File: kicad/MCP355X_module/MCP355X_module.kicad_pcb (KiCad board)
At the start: 2 copper layers, 20.8 x 20.8 mm, 21 parts, among them J1 PINS_1X8, J2 PINS_1X8, U1 MCP355X-E_SN

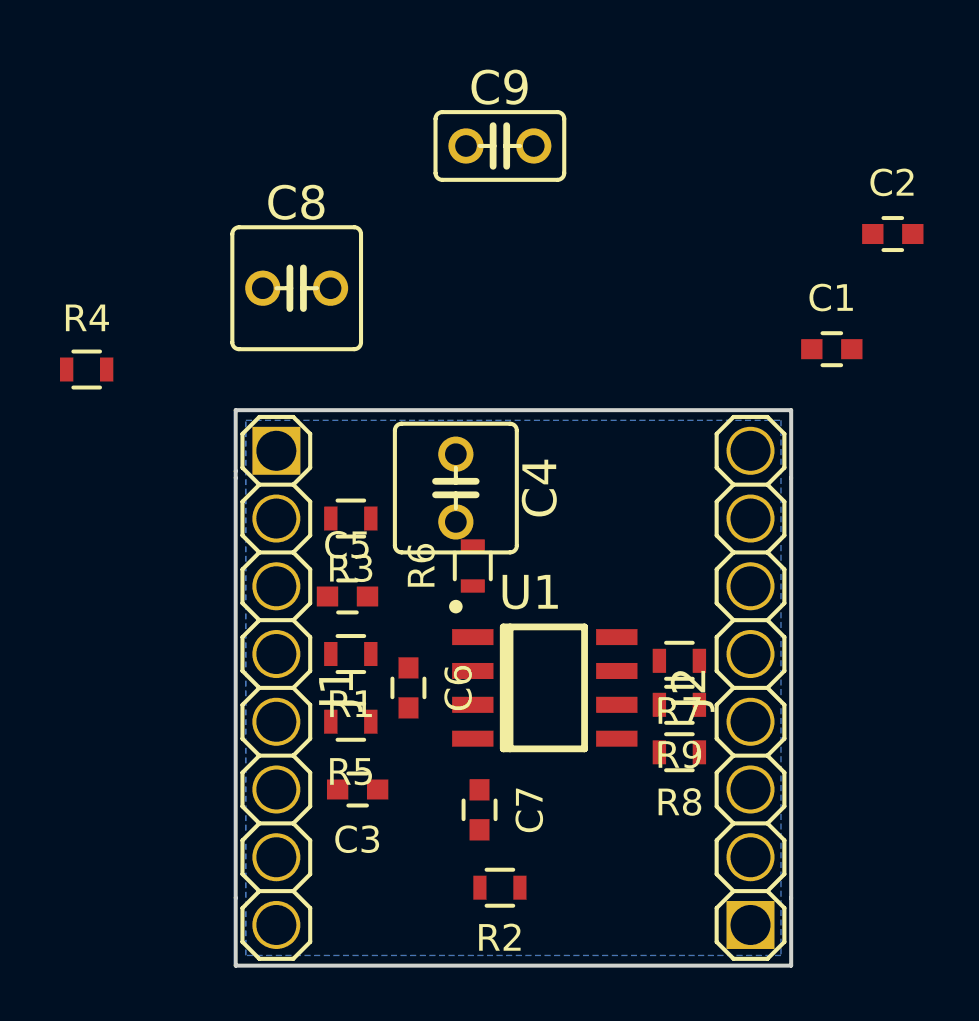
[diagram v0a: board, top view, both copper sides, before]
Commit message: * finished routing MCP355X PCB
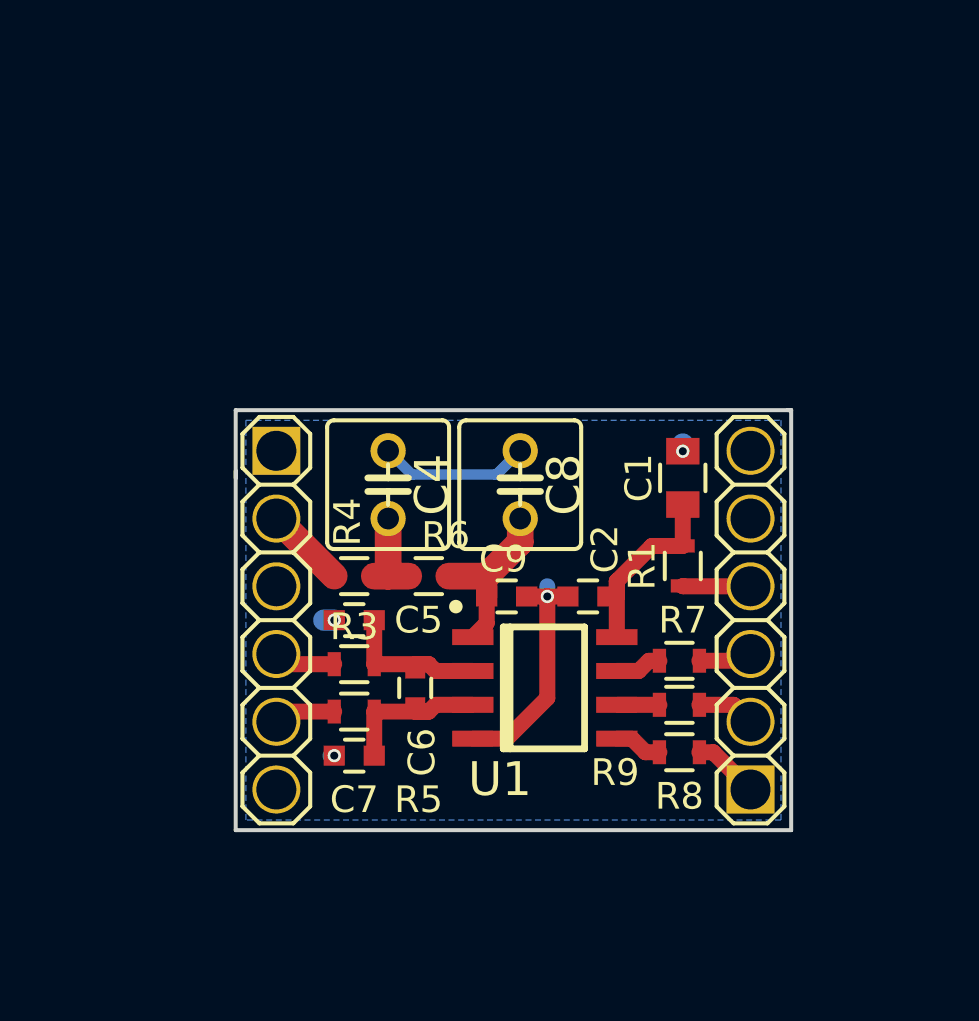
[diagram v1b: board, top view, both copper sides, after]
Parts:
- removed C3: C, Capacitors_SMD:C_0603
- removed R2: R, Resistors_SMD:R_0603
- C1: value C -> 1u; footprint Capacitors_SMD:C_0603 -> Capacitors_SMD:C_0805
- C2: value C -> 10n
- C4, C8: footprint SquantorRcl:SquantorRCL-C025-050X050 -> SquantorRcl:RCL-C025-050X050
- C9: footprint SquantorRcl:SquantorRCL-C025-025X050 -> Capacitors_SMD:C_0603
- J1, J2: value PINS_1X8 -> PINS_1X6; footprint SquantorConnectors:Header-2.54-1X08-H1.5 -> SquantorConnectors:Header-2.54-1X06-H1.5
- R1: value R -> 100
- moved C2 17.8 mm to (153.9, 103.3), turned to 180 degrees
- moved C9 16.9 mm to (150.9, 103.3), turned to 180 degrees
- moved R4 14.9 mm to (145.2, 105.8), turned to 180 degrees
- moved R1 12.9 mm to (157.5, 102.1), turned to 90 degrees
- moved C8 11.2 mm to (151.4, 99.1), turned to 270 degrees
- moved C1 7.38 mm to (157.5, 98.8), turned to 90 degrees
- moved C7 5.12 mm to (145.2, 109.2), turned to 180 degrees
- moved C4 2.54 mm to (146.4, 99.1)
- moved J1 2.54 mm to (142.2, 104.1)
- moved J2 2.54 mm to (160.0, 104.1)
- moved R3 2.16 mm to (145.2, 102.5)
- moved R6 1.69 mm to (148.0, 102.5), turned to 180 degrees
- moved C5 0.92 mm to (145.2, 104.1)
- moved R5 0.40 mm to (145.2, 107.6)
- moved C6 0.25 mm to (147.4, 106.7)
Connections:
- C1 pad 1: GND -> VDD
- C1 pad 2: Net-(C1-Pad2) -> GND
- C2 pad 1: Net-(C1-Pad2) -> VDD
- C2 pad 2: Net-(C2-Pad2) -> GND
- J2 pad 1: (no net) -> Net-(J2-Pad1)
- J2 pad 2: (no net) -> Net-(J2-Pad2)
- J2 pad 5: Net-(J2-Pad5) -> (no net)
- J2 pad 6: VDD -> (no net)
- R1 pad 1: Net-(C1-Pad2) -> Net-(J2-Pad4)
- R1 pad 2: Net-(J1-Pad4) -> VDD
- R7 pad 1: Net-(J2-Pad5) -> Net-(J2-Pad3)
- R8 pad 1: Net-(J2-Pad3) -> Net-(J2-Pad1)
- R9 pad 1: Net-(J2-Pad4) -> Net-(J2-Pad2)
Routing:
- net GND: track 0.00 -> 15.7 mm, vias 0 -> 4
- net VDD: track 0.00 -> 7.58 mm
- net Net-(C8-Pad2): track 0.00 -> 6.60 mm
- net Net-(C5-Pad2): track 0.00 -> 6.10 mm
- net Net-(C6-Pad2): track 0.00 -> 6.10 mm
- net Net-(C4-Pad2): track 0.00 -> 3.45 mm
- net Net-(J1-Pad2): track 0.00 -> 3.07 mm
- net Net-(J1-Pad5): track 0.00 -> 2.87 mm
- net Net-(J1-Pad4): track 0.00 -> 2.87 mm
- net Net-(J2-Pad4): track 0.00 -> 2.54 mm
- net Net-(J2-Pad1): track 0.00 -> 2.50 mm
- net Net-(J2-Pad2): track 0.00 -> 2.18 mm
- net Net-(J2-Pad3): track 0.00 -> 2.02 mm
- net Net-(R8-Pad2): track 0.00 -> 1.81 mm
- net Net-(R7-Pad2): track 0.00 -> 1.75 mm
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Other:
- board size 20.8 x 20.8 mm -> 20.8 x 15.7 mm

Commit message: * added OHSW logo and version
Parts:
- added REF***: OSHW-Logo2_9.8x8mm_SilkScreen, Symbols:OSHW-Logo2_9.8x8mm_SilkScreen, B.Cu at (151.8, 105.8)
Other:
- board text added: "V2016.12.10"

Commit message: * small mods and optimizations
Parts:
- removed REF***: OSHW-Logo2_9.8x8mm_SilkScreen, Symbols:OSHW-Logo2_9.8x8mm_SilkScreen
- J1, J2: footprint SquantorConnectors:Header-2.54-1X06-H1.5 -> SquantorConnectors:Header-2.54-1X06-H0.8
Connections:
- net Net-(C4-Pad2) renamed /Vref_filt
- net Net-(C5-Pad2) renamed /Vin+filt
- net Net-(C6-Pad2) renamed /Vin-_filt
- net Net-(C8-Pad2) renamed /Vref
- net Net-(J1-Pad2) renamed /Vref_in
- net Net-(J1-Pad4) renamed /Vin+_in
- net Net-(J1-Pad5) renamed /Vin-_in
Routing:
- net GND: track 15.7 -> 19.4 mm

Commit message: * again some small modifications
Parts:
- added REF***: OSHW-Logo2_9.8x8mm_SilkScreen, Symbols:OSHW-Logo2_9.8x8mm_SilkScreen, B.Cu at (151.6, 105.5)
- J1, J2: moved to B.Cu

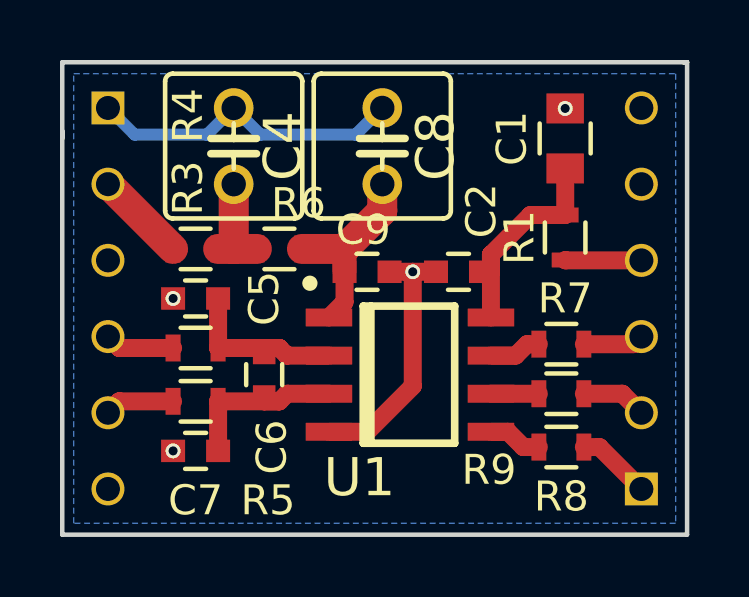
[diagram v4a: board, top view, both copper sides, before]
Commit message: * changed input filter caps from 0603 to 0805
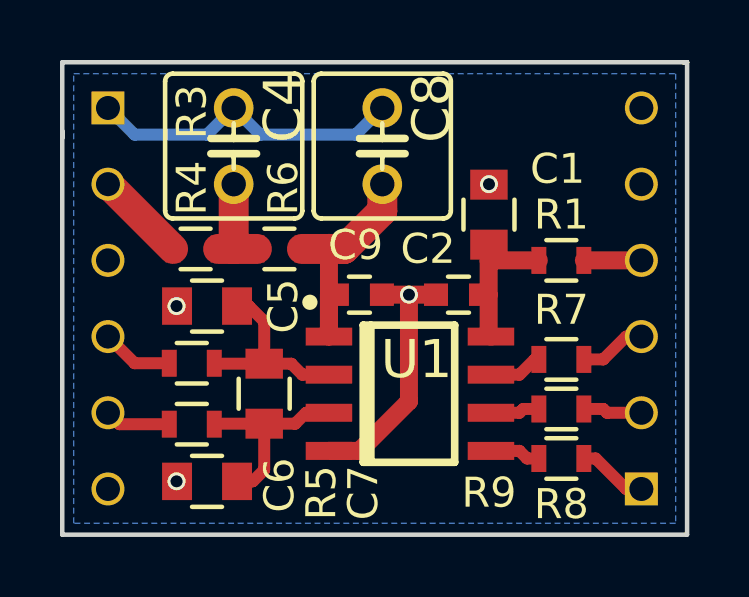
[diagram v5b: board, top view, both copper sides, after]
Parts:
- C5, C6, C7: footprint Capacitors_SMD:C_0603 -> Capacitors_SMD:C_0805
- moved C1 3.59 mm to (154.9, 101.3)
- moved C7 1.09 mm to (145.5, 110.2)
- moved C9 0.80 mm to (150.6, 104.0)
- moved R5 0.77 mm to (145.0, 108.3)
- moved R1 0.77 mm to (157.4, 102.9), turned to 180 degrees
- moved C2 0.76 mm to (153.9, 104.0)
- moved C6 0.63 mm to (147.4, 107.3)
- moved U1 0.63 mm to (152.3, 107.3)
- moved R4 0.52 mm to (145.0, 106.3)
- moved R7 0.51 mm to (157.4, 106.2)
- moved R9 0.51 mm to (157.4, 107.8)
- moved C5 0.46 mm to (145.5, 104.4)
- moved R8 0.38 mm to (157.4, 109.5)
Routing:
- net VDD: track 7.58 -> 4.76 mm
- net /Vref: track 6.60 -> 8.41 mm
- net /Vin-_in: track 2.87 -> 2.20 mm
- net Net-(J2-Pad4): track 2.54 -> 1.92 mm

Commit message: * small mods
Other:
- rule pad_to_mask_clearance: 0.2 -> 0.1
- board text added: "V20161219"
- board text removed: "V2016.12.10"
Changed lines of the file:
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@@
     (links 34)
     (no_connects 0)
-    (area 140.640999 96.190999 161.619001 112.089001)
+    (area 137.095 91.584714 165.375 115.21)
     (thickness 1.6)
     (drawings 7)
@@
   (page A4)
   (layers
-    (0 F.Cu signal)
-    (31 B.Cu signal)
+    (0 F.Cu signal hide)
+    (31 B.Cu signal hide)
     (32 B.Adhes user)
     (33 F.Adhes user)
     (34 B.Paste user)
     (35 F.Paste user)
-    (36 B.SilkS user hide)
+    (36 B.SilkS user)
     (37 F.SilkS user)
     (38 B.Mask user)
@@
   )
   (setup
-    (last_trace_width 0.4)
+    (last_trace_width 0.25)
     (user_trace_width 0.3)
     (user_trace_width 0.4)
@@
     (pad_size 1.524 1.524)
     (pad_drill 0.762)
-    (pad_to_mask_clearance 0.2)
+    (pad_to_mask_clearance 0.1)
     (aux_axis_origin 0 0)
     (visible_elements FFFFFF7F)
@@
     )
   )
-  (gr_text V2016.12.10 (at 151.384 110.49) (layer B.SilkS)
+  (gr_text V20161219 (at 151.638 110.49) (layer B.SilkS)
     (effects (font (size 1.27 1.27) (thickness 0.15)) (justify mirror))
   )

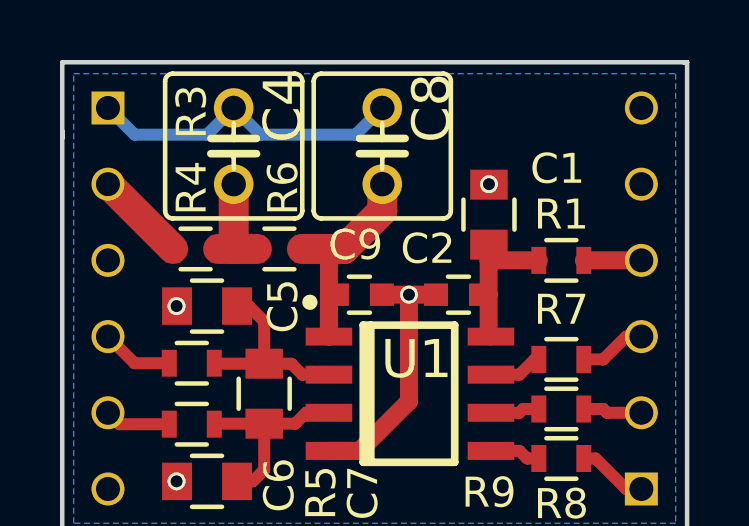
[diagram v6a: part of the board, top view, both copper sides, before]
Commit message: * changed bad footprints for the WIMA MKS-02 1uF caps
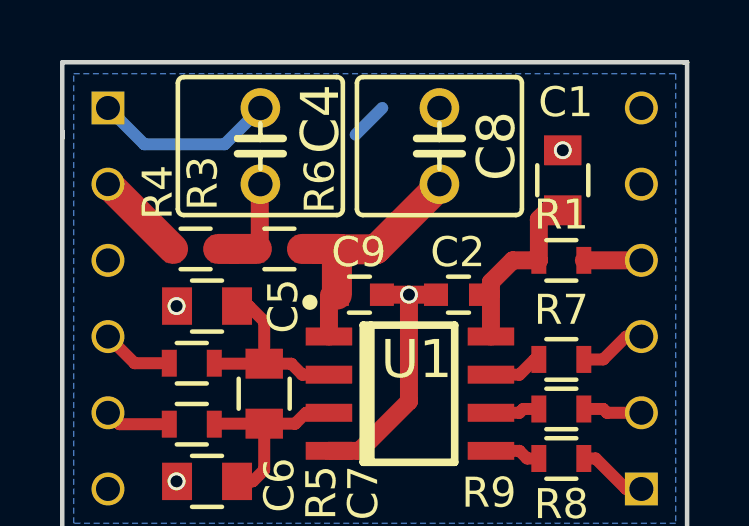
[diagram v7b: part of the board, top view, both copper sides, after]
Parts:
- C4, C8: footprint SquantorRcl:RCL-C025-050X050 -> SquantorRcl:C025-055X046
- moved C1 2.71 mm to (157.4, 100.2)
- moved C8 1.91 mm to (153.3, 99.1)
- moved C4 0.89 mm to (147.3, 99.1)
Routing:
- net GND: track 19.1 -> 15.8 mm
- net VDD: track 4.76 -> 6.34 mm
- net /Vref: track 8.41 -> 8.99 mm
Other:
- board text added: "V20170107"
- board text removed: "V20161219"
